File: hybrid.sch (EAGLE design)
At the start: 122 parts, among them IC1 TL071P, IC2 TL071P, IC3 LM317MABT, IC4 LM317MABT, J1 RCJ-21XXMILL, J2 NRJ3HF-1, J3 703W-00/54, Q1 BC560KINKED, Q10 BC560KINKED, Q11 BC560KINKED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

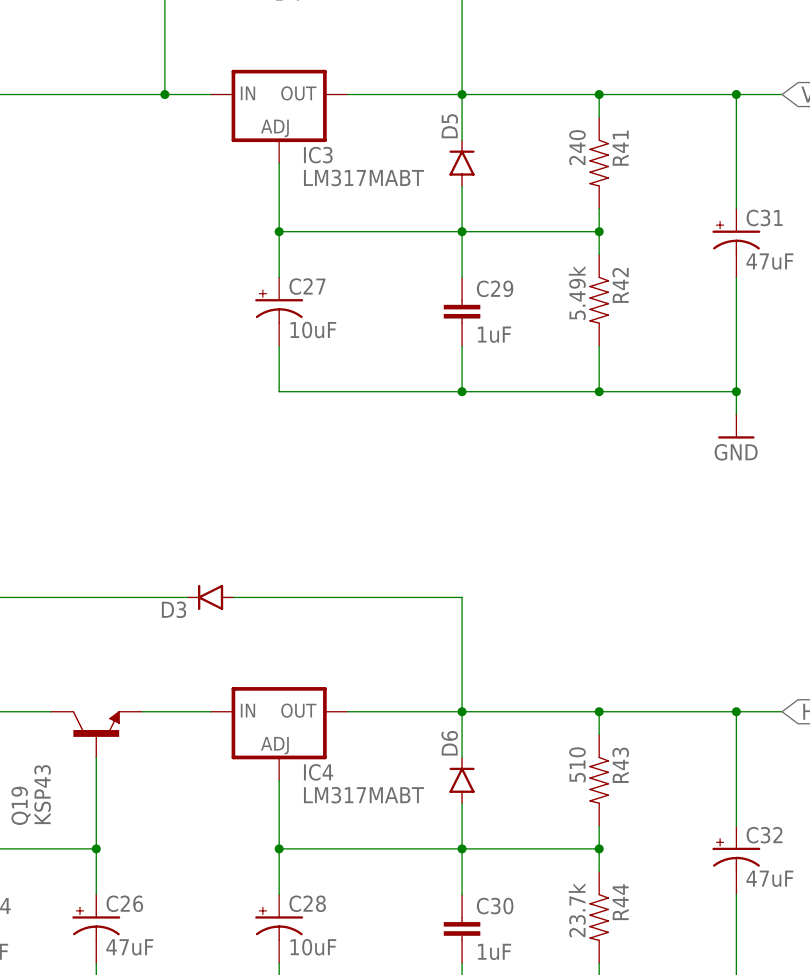
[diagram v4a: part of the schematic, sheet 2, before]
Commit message: No silk for vregs
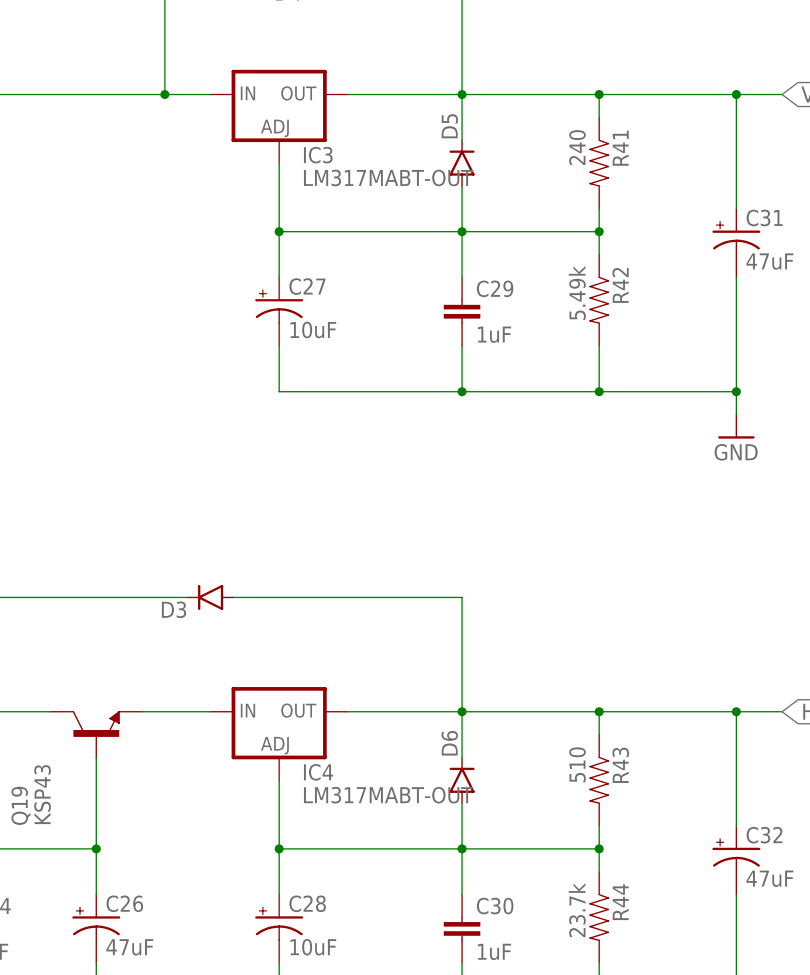
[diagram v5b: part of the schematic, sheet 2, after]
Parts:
- IC3, IC4: value LM317MABT -> LM317MABT-OUT; device v-reg:LM317MABT -> my-reg:LM317MABT-OUT
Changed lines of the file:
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@@
 <grid distance="0.1" unitdist="inch" unit="inch" style="lines" multiple="1" display="no" altdistance="0.01" altunitdist="inch" altunit="inch"/>
 <layers>
-<layer number="1" name="Top" color="4" fill="1" visible="yes" active="no"/>
-<layer number="2" name="Route2" color="1" fill="3" visible="yes" active="no"/>
-<layer number="3" name="Route3" color="4" fill="3" visible="yes" active="no"/>
-<layer number="4" name="Route4" color="1" fill="4" visible="yes" active="no"/>
-<layer number="5" name="Route5" color="4" fill="4" visible="yes" active="no"/>
-<layer number="6" name="Route6" color="1" fill="8" visible="yes" active="no"/>
-<layer number="7" name="Route7" color="4" fill="8" visible="yes" active="no"/>
-<layer number="8" name="Route8" color="1" fill="2" visible="yes" active="no"/>
-<layer number="9" name="Route9" color="4" fill="2" visible="yes" active="no"/>
-<layer number="10" name="Route10" color="1" fill="7" visible="yes" active="no"/>
-<layer number="11" name="Route11" color="4" fill="7" visible="yes" active="no"/>
-<layer number="12" name="Route12" color="1" fill="5" visible="yes" active="no"/>
-<layer number="13" name="Route13" color="4" fill="5" visible="yes" active="no"/>
-<layer number="14" name="Route14" color="1" fill="6" visible="yes" active="no"/>
-<layer number="15" name="Route15" color="4" fill="6" visible="yes" active="no"/>
-<layer number="16" name="Bottom" color="1" fill="1" visible="yes" active="no"/>
-<layer number="17" name="Pads" color="2" fill="1" visible="yes" active="no"/>
-<layer number="18" name="Vias" color="2" fill="1" visible="yes" active="no"/>
-<layer number="19" name="Unrouted" color="6" fill="1" visible="yes" active="no"/>
-<layer number="20" name="Dimension" color="15" fill="1" visible="yes" active="no"/>
-<layer number="21" name="tPlace" color="7" fill="1" visible="yes" active="no"/>
-<layer number="22" name="bPlace" color="7" fill="1" visible="yes" active="no"/>
-<layer number="23" name="tOrigins" color="15" fill="1" visible="yes" active="no"/>
-<layer number="24" name="bOrigins" color="15" fill="1" visible="yes" active="no"/>
-<layer number="25" name="tNames" color="7" fill="1" visible="yes" active="no"/>
-<layer number="26" name="bNames" color="7" fill="1" visible="yes" active="no"/>
-<layer number="27" name="tValues" color="7" fill="1" visible="yes" active="no"/>
-<layer number="28" name="bValues" color="7" fill="1" visible="yes" active="no"/>
+<layer number="1" name="Top" color="4" fill="1" visible="no" active="no"/>
+<layer number="2" name="Route2" color="1" fill="3" visible="no" active="no"/>
+<layer number="3" name="Route3" color="4" fill="3" visible="no" active="no"/>
+<layer number="4" name="Route4" color="1" fill="4" visible="no" active="no"/>
+<layer number="5" name="Route5" color="4" fill="4" visible="no" active="no"/>
+<layer number="6" name="Route6" color="1" fill="8" visible="no" active="no"/>
+<layer number="7" name="Route7" color="4" fill="8" visible="no" active="no"/>
+<layer number="8" name="Route8" color="1" fill="2" visible="no" active="no"/>
+<layer number="9" name="Route9" color="4" fill="2" visible="no" active="no"/>
+<layer number="10" name="Route10" color="1" fill="7" visible="no" active="no"/>
+<layer number="11" name="Route11" color="4" fill="7" visible="no" active="no"/>
+<layer number="12" name="Route12" color="1" fill="5" visible="no" active="no"/>
+<layer number="13" name="Route13" color="4" fill="5" visible="no" active="no"/>
+<layer number="14" name="Route14" color="1" fill="6" visible="no" active="no"/>
+<layer number="15" name="Route15" color="4" fill="6" visible="no" active="no"/>
+<layer number="16" name="Bottom" color="1" fill="1" visible="no" active="no"/>
+<layer number="17" name="Pads" color="2" fill="1" visible="no" active="no"/>
+<layer number="18" name="Vias" color="2" fill="1" visible="no" active="no"/>
+<layer number="19" name="Unrouted" color="6" fill="1" visible="no" active="no"/>
+<layer number="20" name="Dimension" color="15" fill="1" visible="no" active="no"/>
+<layer number="21" name="tPlace" color="7" fill="1" visible="no" active="no"/>
+<layer number="22" name="bPlace" color="7" fill="1" visible="no" active="no"/>
+<layer number="23" name="tOrigins" color="15" fill="1" visible="no" active="no"/>
+<layer number="24" name="bOrigins" color="15" fill="1" visible="no" active="no"/>
+<layer number="25" name="tNames" color="7" fill="1" visible="no" active="no"/>
+<layer number="26" name="bNames" color="7" fill="1" visible="no" active="no"/>
+<layer number="27" name="tValues" color="7" fill="1" visible="no" active="no"/>
+<layer number="28" name="bValues" color="7" fill="1" visible="no" active="no"/>
 <layer number="29" name="tStop" color="7" fill="3" visible="no" active="no"/>
 <layer number="30" name="bStop" color="7" fill="6" visible="no" active="no"/>
@@
 <layer number="35" name="tGlue" color="7" fill="4" visible="no" active="no"/>
 <layer number="36" name="bGlue" color="7" fill="5" visible="no" active="no"/>
-<layer number="37" name="tTest" color="7" fill="1" visible="yes" active="no"/>
-<layer number="38" name="bTest" color="7" fill="1" visible="yes" active="no"/>
+<layer number="37" name="tTest" color="7" fill="1" visible="no" active="no"/>
+<layer number="38" name="bTest" color="7" fill="1" visible="no" active="no"/>
 <layer number="39" name="tKeepout" color="4" fill="11" visible="no" active="no"/>
 <layer number="40" name="bKeepout" color="1" fill="11" visible="no" active="no"/>
@@
 <layer number="44" name="Drills" color="7" fill="1" visible="no" active="no"/>
 <layer number="45" name="Holes" color="7" fill="1" visible="no" active="no"/>
-<layer number="46" name="Milling" color="3" fill="1" visible="yes" active="no"/>
-<layer number="47" name="Measures" color="7" fill="1" visible="yes" active="no"/>
-<layer number="48" name="Document" color="7" fill="1" visible="yes" active="no"/>
-<layer number="49" name="Reference" color="7" fill="1" visible="yes" active="no"/>
-<layer number="50" name="dxf" color="7" fill="1" visible="yes" active="no"/>
-<layer number="51" name="tDocu" color="7" fill="1" visible="yes" active="no"/>
-<layer number="52" name="bDocu" color="7" fill="1" visible="yes" active="no"/>
-<layer number="53" name="tGND_GNDA" color="7" fill="9" visible="yes" active="no"/>
-<layer number="54" name="bGND_GNDA" color="1" fill="9" visible="yes" active="no"/>
-<layer number="56" name="wert" color="7" fill="1" visible="yes" active="no"/>
-<layer number="57" name="tCAD" color="7" fill="1" visible="yes" active="no"/>
-<layer number="59" name="tCarbon" color="7" fill="1" visible="yes" active="no"/>
-<layer number="60" name="bCarbon" color="7" fill="1" visible="yes" active="no"/>
+<layer number="46" name="Milling" color="3" fill="1" visible="no" active="no"/>
+<layer number="47" name="Measures" color="7" fill="1" visible="no" active="no"/>
+<layer number="48" name="Document" color="7" fill="1" visible="no" active="no"/>
+<layer number="49" name="Reference" color="7" fill="1" visible="no" active="no"/>
+<layer number="50" name="dxf" color="7" fill="1" visible="no" active="no"/>
+<layer number="51" name="tDocu" color="7" fill="1" visible="no" active="no"/>
+<layer number="52" name="bDocu" color="7" fill="1" visible="no" active="no"/>
+<layer number="53" name="tGND_GNDA" color="7" fill="9" visible="no" active="no"/>
+<layer number="54" name="bGND_GNDA" color="1" fill="9" visible="no" active="no"/>
+<layer number="56" name="wert" color="7" fill="1" visible="no" active="no"/>
+<layer number="57" name="tCAD" color="7" fill="1" visible="no" active="no"/>
+<layer number="59" name="tCarbon" color="7" fill="1" visible="no" active="no"/>
+<layer number="60" name="bCarbon" color="7" fill="1" visible="no" active="no"/>
 <layer number="90" name="Modules" color="5" fill="1" visible="yes" active="yes"/>
 <layer number="91" name="Nets" color="2" fill="1" visible="yes" active="yes"/>
@@
 <part name="R25" library="SparkFun-Resistors" deviceset="RESISTOR" device="PTH-1/4W" value="1Meg"/>
 <part name="GND19" library="SparkFun-Aesthetics" deviceset="GND" device=""/>
-<part name="IC3" library="v-reg" deviceset="LM317?*" device="MABT"/>
+<part name="IC3" library="my-reg" deviceset="LM317?*" device="MABT-OUT"/>
 <part name="C23" library="my-cap" deviceset="CAP_POL" device="SNAPIN-30/10" value="4700uF"/>
 <part name="GND26" library="SparkFun-Aesthetics" deviceset="GND" device=""/>
@@
 <part name="D1" library="SparkFun-DiscreteSemi" deviceset="DIODE" device="PTH"/>
 <part name="GND27" library="SparkFun-Aesthetics" deviceset="GND" device=""/>
-<part name="IC4" library="v-reg" deviceset="LM317?*" device="MABT"/>
+<part name="IC4" library="my-reg" deviceset="LM317?*" device="MABT-OUT"/>
 <part name="R44" library="SparkFun-Resistors" deviceset="RESISTOR" device="PTH-1/4W" value="23.7k"/>
 <part name="R43" library="SparkFun-Resistors" deviceset="RESISTOR" device="PTH-1/4W" value="510"/>

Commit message: Values fixed
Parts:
- R39: value 0.549 -> 0.51
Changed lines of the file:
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@@
 <?xml version="1.0" encoding="utf-8"?>
 <!DOCTYPE eagle SYSTEM "eagle.dtd">
-<eagle version="8.0.1">
+<eagle version="8.0.2">
 <drawing>
 <settings>
@@
 <part name="A1" library="my-smps" deviceset="R-78HBXX-0.5" device=""/>
 <part name="GND28" library="SparkFun-Aesthetics" deviceset="GND" device=""/>
-<part name="R39" library="my-res" deviceset="RESISTOR" device="PTH-1/2W" value="0.549"/>
+<part name="R39" library="my-res" deviceset="RESISTOR" device="PTH-1/2W" value="0.51"/>
 <part name="GB1" library="my" deviceset="COPPER-BRIDGE" device="SM" value=""/>
 <part name="GND29" library="SparkFun-Aesthetics" deviceset="GND" device=""/>
